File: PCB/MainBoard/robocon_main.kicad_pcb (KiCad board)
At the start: 2 copper layers, 6 parts, among them U2 RP2040, U3 TB67H450, U5 TB67H450, U6 TB67H450, U7 TB67H450, U8 BNO055

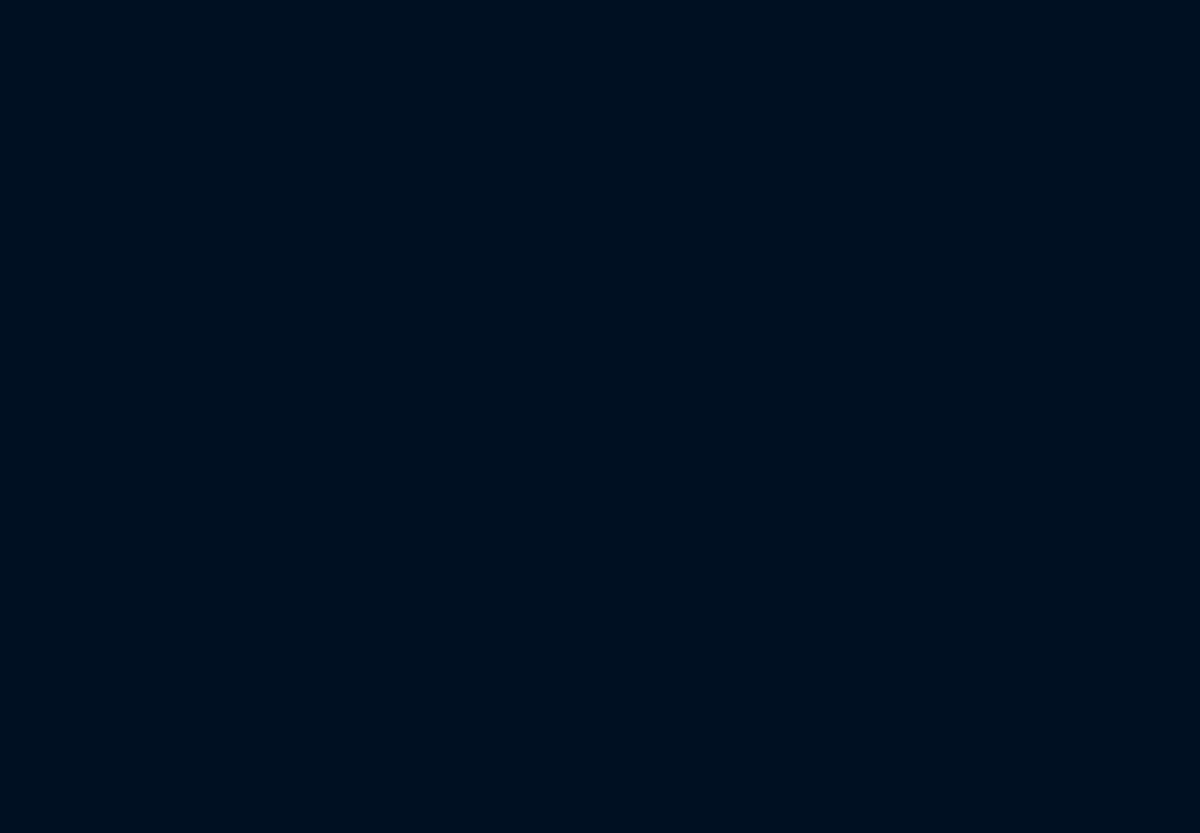
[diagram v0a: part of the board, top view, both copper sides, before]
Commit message: サーボ、ラインセンサのコネクタ化、ラベル更新
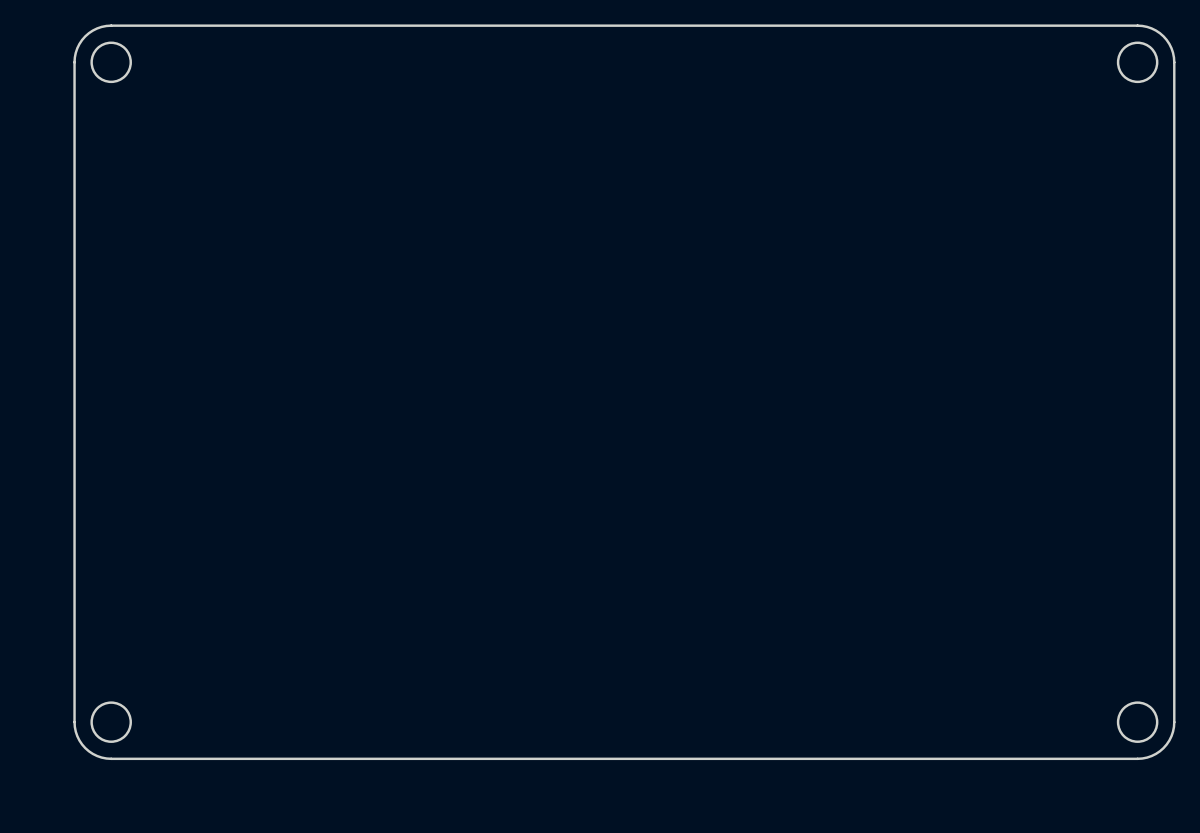
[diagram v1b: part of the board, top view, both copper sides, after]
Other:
- board outline added: 90 x 60 mm
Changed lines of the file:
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@@
 		(embedded_fonts no)
+	)
+	(gr_line
+		(start 177.000001 85.499999)
+		(end 261 85.499999)
+		(stroke
+			(width 0.2)
+			(type default)
+		)
+		(layer "Edge.Cuts")
+	)
+	(gr_circle
+		(center 261 82.499999)
+		(end 262.6 82.499999)
+		(stroke
+			(width 0.2)
+			(type default)
+		)
+		(fill no)
+		(layer "Edge.Cuts")
+	)
+	(gr_circle
+		(center 177 82.499999)
+		(end 178.6 82.499999)
+		(stroke
+			(width 0.2)
+			(type default)
+		)
+		(fill no)
+		(layer "Edge.Cuts")
+	)
+	(gr_arc
+		(start 177.000001 85.499999)
+		(mid 174.87868 84.621319)
+		(end 174 82.499998)
+		(stroke
+			(width 0.2)
+			(type default)
+		)
+		(layer "Edge.Cuts")
+	)
+	(gr_line
+		(start 174 28.5)
+		(end 174 82.499998)
+		(stroke
+			(width 0.2)
+			(type default)
+		)
+		(layer "Edge.Cuts")
+	)
+	(gr_line
+		(start 260.999999 25.499999)
+		(end 177.000001 25.499999)
+		(stroke
+			(width 0.2)
+			(type default)
+		)
+		(layer "Edge.Cuts")
+	)
+	(gr_arc
+		(start 174 28.5)
+		(mid 174.87868 26.378679)
+		(end 177.000001 25.499999)
+		(stroke
+			(width 0.2)
+			(type default)
+		)
+		(layer "Edge.Cuts")
+	)
+	(gr_circle
+		(center 177 28.499999)
+		(end 178.6 28.499999)
+		(stroke
+			(width 0.2)
+			(type default)
+		)
+		(fill no)
+		(layer "Edge.Cuts")
+	)
+	(gr_line
+		(start 264 82.499998)
+		(end 264 28.5)
+		(stroke
+			(width 0.2)
+			(type default)
+		)
+		(layer "Edge.Cuts")
+	)
+	(gr_arc
+		(start 260.999999 25.499999)
+		(mid 263.12132 26.378679)
+		(end 264 28.5)
+		(stroke
+			(width 0.2)
+			(type default)
+		)
+		(layer "Edge.Cuts")
+	)
+	(gr_arc
+		(start 264 82.499998)
+		(mid 263.12132 84.621319)
+		(end 261 85.499999)
+		(stroke
+			(width 0.2)
+			(type default)
+		)
+		(layer "Edge.Cuts")
+	)
+	(gr_circle
+		(center 261 28.499999)
+		(end 262.6 28.499999)
+		(stroke
+			(width 0.2)
+			(type default)
+		)
+		(fill no)
+		(layer "Edge.Cuts")
 	)
 	(segment
@@
 		(net 17)
 	)
+	(group ""
+		(members "0b14ea96-bd6d-4c90-b475-0f61661f05f3" "41c4f6dd-afa6-4a23-a0eb-7e419133f33c"
+			"730f7db8-25f3-4cd7-b36e-fb8d70e98300" "9ab15159-e839-4613-8b9e-deb2075557dc"
+			"a069409f-41e9-4e9c-a7bc-f38278514d84" "b522c5fe-c24b-4e3f-b514-eac5c4825775"
+			"b9575a36-5020-4aa9-8a55-d26479d1f17e" "c2f965af-dc2f-46f2-8a15-c4c280d2a0ed"
+			"cfd8b63c-2895-498d-a8f8-e72353d947f4" "d21b8abd-dfbf-4855-b696-573351d8b1c7"
+			"e090b8f6-31d4-47ba-b858-d51f2ca9b6ab" "e6f12c6b-7d4b-4a27-9fb3-744be783c98a"
+		)
+	)
 	(embedded_fonts no)

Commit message: 発注用データ
GitHubデスクトップ直った！
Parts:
- added 12V: LED, LED_SMD:LED_0603_1608Metric_Pad1.05x0.95mm_HandSolder, F.Cu at (145.7, 81.9)
- added 3V3: LED, LED_SMD:LED_0603_1608Metric_Pad1.05x0.95mm_HandSolder, F.Cu at (145.6, 87.5)
- added 5V: LED, LED_SMD:LED_0603_1608Metric_Pad1.05x0.95mm_HandSolder, F.Cu at (145.6, 84.9)
- added C1: 0.33μF, Capacitor_SMD:C_0603_1608Metric_Pad1.08x0.95mm_HandSolder, F.Cu at (151.9, 101.1)
- added C2: 2.2μF, Capacitor_SMD:C_0603_1608Metric_Pad1.08x0.95mm_HandSolder, F.Cu at (156.6, 101.0)
- added C3: 10μF, Capacitor_SMD:C_1206_3216Metric_Pad1.33x1.80mm_HandSolder, F.Cu at (158.2, 66.6)
- added D4: LED, LED_SMD:LED_0603_1608Metric_Pad1.05x0.95mm_HandSolder, F.Cu at (145.8, 94.4)
- added D5: LED, LED_SMD:LED_0603_1608Metric_Pad1.05x0.95mm_HandSolder, F.Cu at (146.0, 97.2)
- added D6: LED, LED_SMD:LED_0603_1608Metric_Pad1.05x0.95mm_HandSolder, F.Cu at (146.1, 99.4)
- added D7: LED, LED_SMD:LED_0603_1608Metric_Pad1.05x0.95mm_HandSolder, F.Cu at (145.8, 102.0)
- added D8: D, my_footprints_library:MA10EB045, B.Cu at (145.6, 90.7)
- added D9: D, my_footprints_library:MA10EB045, F.Cu at (153.1, 82.8)
- added F1: 3557-15, my_footprints_library:3557-15_KEY, F.Cu at (134.2, 60.8)
- added J1: DC2_OUT, Connector_JST:JST_XA_B02B-XASK-1-A_1x02_P2.50mm_Vertical, F.Cu at (106.4, 83.3)
- added J12: to_MUX, Connector_JST:JST_PH_B5B-PH-K_1x05_P2.00mm_Vertical, F.Cu at (187.8, 94.7)
- added J13: to_OKL-T/6-W12N-C, Connector_Wire:SolderWirePad_1x01_SMD_3x6mm, B.Cu at (140.3, 69.1)
- added J14: from_OKL-T/6-W12N-C, Connector_Wire:SolderWirePad_1x01_SMD_3x6mm, B.Cu at (135.1, 111.7)
- added J15: Conn_01x02_Pin, Connector_JST:JST_PH_B6B-PH-K_1x06_P2.00mm_Vertical, F.Cu at (109.8, 114.7)
- added J2: POWER, Connector_AMASS:AMASS_XT30U-M_1x02_P5.0mm_Vertical, F.Cu at (120.6, 61.9)
- added J3: DC1_OUT, Connector_JST:JST_XA_B02B-XASK-1-A_1x02_P2.50mm_Vertical, F.Cu at (106.2, 68.8)
- added J4: to_COLOR, Connector_JST:JST_PH_B5B-PH-K_1x05_P2.00mm_Vertical, F.Cu at (188.0, 67.9)
- added J5: DC3_OUT, Connector_JST:JST_XA_B02B-XASK-1-A_1x02_P2.50mm_Vertical, F.Cu at (106.3, 94.0)
- added J6: to_SERVO1, Connector_PinHeader_2.54mm:PinHeader_1x03_P2.54mm_Vertical, F.Cu at (181.8, 113.7)
- added J7: DC4_OUT, Connector_JST:JST_XA_B02B-XASK-1-A_1x02_P2.50mm_Vertical, F.Cu at (106.2, 106.2)
- added J8: to_SERVO2, Connector_PinHeader_2.54mm:PinHeader_1x03_P2.54mm_Vertical, F.Cu at (177.8, 113.7)
- added J9: to_CAM, Connector:NS-Tech_Grove_1x04_P2mm_Vertical, F.Cu at (187.3, 82.5)
- added POW: POW, my_footprints_library:1P2T_toggle, F.Cu at (151.0, 75.8)
- added R1: R, Resistor_SMD:R_0603_1608Metric_Pad0.98x0.95mm_HandSolder, F.Cu at (141.1, 82.4)
- added R2: R, Resistor_SMD:R_0603_1608Metric_Pad0.98x0.95mm_HandSolder, F.Cu at (141.1, 84.9)
- added R3: R, Resistor_SMD:R_0603_1608Metric_Pad0.98x0.95mm_HandSolder, F.Cu at (141.1, 87.4)
- added R4: R, Resistor_SMD:R_0603_1608Metric_Pad0.98x0.95mm_HandSolder, F.Cu at (141.2, 94.4)
- added R5: R, Resistor_SMD:R_0603_1608Metric_Pad0.98x0.95mm_HandSolder, F.Cu at (141.2, 96.9)
- added R6: R, Resistor_SMD:R_0603_1608Metric_Pad0.98x0.95mm_HandSolder, F.Cu at (141.2, 99.4)
- added R7: R, Resistor_SMD:R_0603_1608Metric_Pad0.98x0.95mm_HandSolder, F.Cu at (141.2, 101.9)
- added R8: R, Resistor_SMD:R_0603_1608Metric_Pad0.98x0.95mm_HandSolder, F.Cu at (154.3, 105.8)
- added R9: R, Resistor_SMD:R_0603_1608Metric_Pad0.98x0.95mm_HandSolder, F.Cu at (146.2, 105.7)
- added REF**: SolderWirePad_1x01_SMD_3x6mm, Connector_Wire:SolderWirePad_1x01_SMD_3x6mm, B.Cu at (150.4, 69.1)
- added REF**: SolderWirePad_1x01_SMD_3x6mm, Connector_Wire:SolderWirePad_1x01_SMD_3x6mm, B.Cu at (125.6, 111.6)
- added TACT1: SW_Push, Button_Switch_THT:SW_PUSH_6mm_H7.3mm, F.Cu at (152.2, 116.0)
- added TACT2: SW_Push, Button_Switch_THT:SW_PUSH_6mm_H7.3mm, F.Cu at (143.9, 116.0)
- added TP1: TestPoint, TestPoint:TestPoint_Pad_2.0x2.0mm, F.Cu at (153.8, 60.4)
- added TP2: TestPoint, TestPoint:TestPoint_Pad_2.0x2.0mm, F.Cu at (158.2, 60.4)
- added U4: 3-Terminal Regulator, Package_TO_SOT_SMD:TO-252-3_TabPin2, F.Cu at (153.7, 90.0)
- moved U2 93.8 mm to (171.0, 81.1)
- moved U3 82.9 mm to (125.6, 70.8), turned to 180 degrees
- moved U5 79.0 mm to (126.2, 84.1), turned to 180 degrees
- moved U6 77.5 mm to (126.2, 94.1), turned to 180 degrees
- moved U7 76.7 mm to (126.3, 102.1), turned to 180 degrees
- moved U8 36.2 mm to (166.2, 111.0), turned to 180 degrees
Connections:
- net /PWM1 renamed /DC_PWM1
- net /PWM2 renamed /DC_PWM2
- net /PWM3 renamed /DC_PWM3
- net /PWM4 renamed /DC_PWM4
- net /PWM5 renamed /DC_PWM5
- net /PWM6 renamed /DC_PWM6
- net /PWM7 renamed /DC_PWM7
- net /PWM8 renamed /DC_PWM8
- U2 pad 14: /SERVO_SIG1 -> /DEBUG_LED1
- U2 pad 15: /SERVO_SIG2 -> /DEBUG_LED2
- U2 pad 16: /SERVO_SIG3 -> /DEBUG_LED3
- U2 pad 17: /SERVO_SIG4 -> /DEBUG_LED4
- U2 pad 19: /LINE_SIG1 -> /MUX_S1
- U2 pad 20: /LINE_SIG2 -> /MUX_S0
- U2 pad 21: /LINE_SIG3 -> /SERVO_PWM1
- U2 pad 22: /LINE_SIG4 -> /SERVO_PWM2
- U2 pad 23: unconnected-(U2-IO20-Pad23) -> /TACT_SW1
- U2 pad 24: unconnected-(U2-IO21-Pad24) -> /TACT_SW2
- U2 pad 25: unconnected-(U2-IO22-Pad25) -> /NchFET_3
- U2 pad 26: unconnected-(U2-IO23-Pad26) -> /NchFET_2
- U2 pad 27: unconnected-(U2-IO24-Pad27) -> /NchFET_1
- U2 pad 28: unconnected-(U2-IO25-Pad28) -> /PchFET
- U2 pad 29: unconnected-(U2-ADC0-Pad29) -> /ANALOG_LINE
- U2 pad 30: unconnected-(U2-ADC1-Pad30) -> /COLOR_B
- U2 pad 31: unconnected-(U2-ADC2-Pad31) -> /COLOR_G
- U2 pad 32: unconnected-(U2-ADC3-Pad32) -> /COLOR_R
- U5 pad 4: unconnected-(U5-VREF-Pad4) -> +3.3V
- U6 pad 4: unconnected-(U6-VREF-Pad4) -> +3.3V
- U7 pad 4: unconnected-(U7-VREF-Pad4) -> +3.3V
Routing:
- net +3.3V: track 0.00 -> 273.7 mm, vias 0 -> 4
- net +12V: track 0.00 -> 173.9 mm, vias 0 -> 5
- net +5V: track 0.00 -> 155.2 mm, vias 0 -> 2
- net /PchFET: track 0.00 -> 90.7 mm, vias 0 -> 2
- net /NchFET_1: track 0.00 -> 88.2 mm, vias 0 -> 2
- net /NchFET_2: track 0.00 -> 81.8 mm, vias 0 -> 1
- net /NchFET_3: track 0.00 -> 78.7 mm, vias 0 -> 2
- net /TACT_SW2: track 0.00 -> 73.4 mm, vias 0 -> 2
- net /TACT_SW1: track 0.00 -> 59.8 mm, vias 0 -> 3
- net /DC_PWM7: track 0.00 -> 38.1 mm, vias 0 -> 2
- net /DC_PWM3: track 0.00 -> 36.1 mm
- net /DC_PWM5: track 0.00 -> 36.1 mm, vias 0 -> 2
- net /DC_PWM8: track 0.00 -> 35.9 mm, vias 0 -> 3
- net /DC_PWM4: track 0.00 -> 33.6 mm
- net /CAM_RX: track 0.00 -> 33.2 mm, vias 0 -> 2
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- added copper zone on B.Cu, net GND
- added copper zone on F.Cu, net GND
- added copper zone on F.Cu, net Net-(J2-Pin_2)
- added copper zone on F.Cu, net Net-(SW1-B)
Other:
- outline, holes or cut-outs redrawn
- board text added: "SOLENOID"
